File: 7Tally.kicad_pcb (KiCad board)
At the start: 4 copper layers, 22 parts, among them J1 53047-0210, P1 53047-0310, SW1 TL3300CF160Q, U1 ESP32-C3_SUPERMINI_TH, U2 BQ21040DBVR, U3 TC1263-3.3VOA

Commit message: chore(PCB): added 3D models and start PCB
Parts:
- removed D3: US1M, Diode_SMD:D_SMA
- removed J1: 53047-0210, 53047-0210:MOLEX_53047-0210
- added D4: ESD7351XV2T1G, ESD7351XV2T1G:SOD-523-2_ONSEMI, F.Cu at (24.7, 45.7)
- added J2: B2B-PH-K-S_LF__SN_, B2B-PH-K-S_LF__SN_:JST_B2B-PH-K-S_LF__SN_, B.Cu at (88.9, 73.7)
- moved U1 108.4 mm to (63.2, 63.5), turned to 90 degrees
- moved U2 72.9 mm to (80.0, 37.1)
- moved SW1 71.5 mm to (82.7, 63.3), turned to 180 degrees
- moved D1 56.0 mm to (72.7, 50.8), turned to 180 degrees
- moved P1 55.6 mm to (59.7, 52.6), turned to 180 degrees
- moved U3 29.5 mm to (61.0, 38.1)
- moved D2 13.6 mm to (26.3, 48.3)
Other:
- board outline added: 42 x 25.4 mm

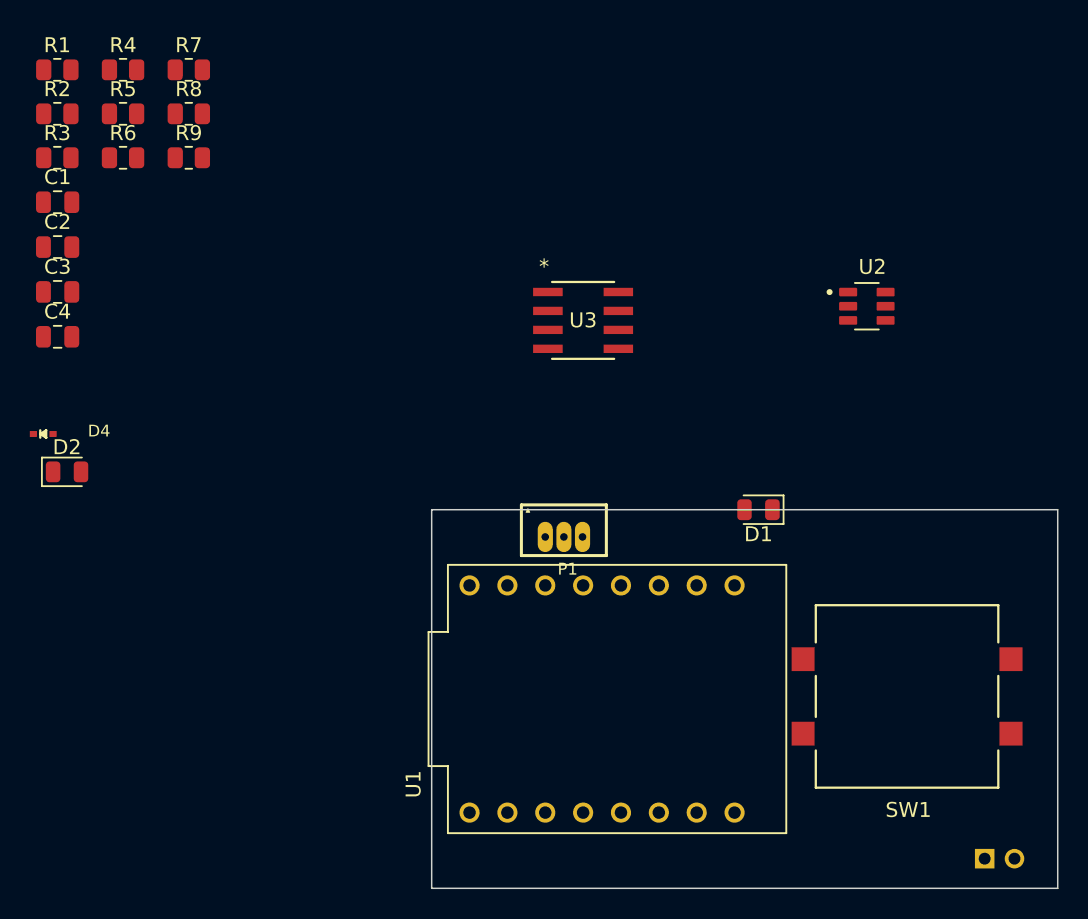
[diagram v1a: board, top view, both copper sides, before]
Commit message: feat(PCB): start of routing
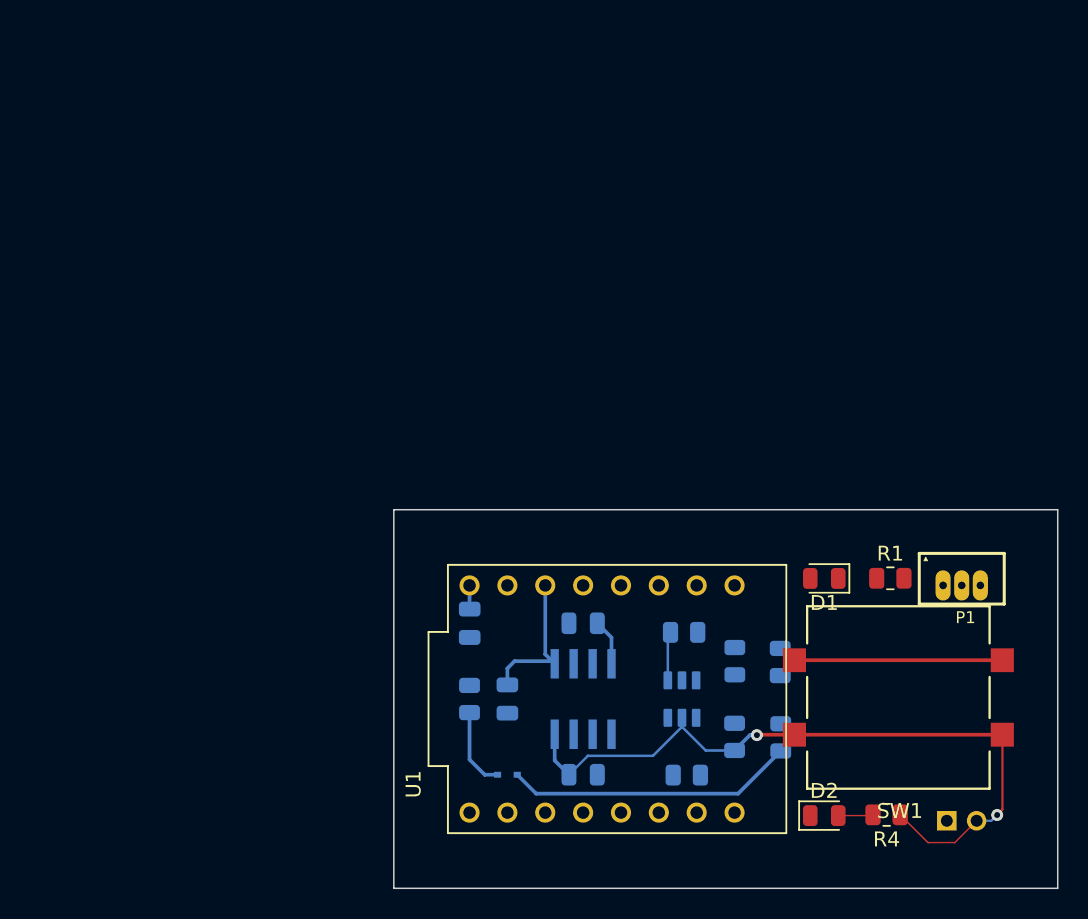
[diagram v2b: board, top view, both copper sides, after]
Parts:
- C1, C2, C3, C4, D4, R2, R3, R5, R6, R7, R8, R9, U2, U3: moved to B.Cu
- moved R4 71.6 mm to (81.3, 71.3), turned to 180 degrees
- moved R1 65.5 mm to (81.6, 55.4)
- moved R5 60.8 mm to (74.2, 66.1), turned to 90 degrees
- moved R3 59.1 mm to (67.9, 68.6), turned to 180 degrees
- moved R7 57.8 mm to (71.1, 66.0), turned to 90 degrees
- moved D2 55.8 mm to (77.1, 71.3)
- moved R6 55.6 mm to (74.2, 61.0), turned to 90 degrees
- moved R2 54.6 mm to (67.7, 59.0)
- moved C1 52.1 mm to (61.0, 68.6)
- moved R8 51.9 mm to (71.1, 61.0), turned to 90 degrees
- moved R9 40.9 mm to (53.3, 63.5), turned to 90 degrees
- moved C3 40.7 mm to (55.9, 63.5), turned to -90 degrees
- moved C4 40.2 mm to (61.0, 58.4), turned to 180 degrees
- moved D4 38.6 mm to (55.9, 68.6)
- moved C2 37.4 mm to (53.4, 58.4), turned to -90 degrees
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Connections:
- U3 pad 2: unconnected-(U3-GND-Pad2) -> GND
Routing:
- net VBAT: track 0.00 -> 48.8 mm, vias 0 -> 2
- net Net-(D4-Pad2): track 0.00 -> 33.3 mm
- net +3.3V: track 0.00 -> 10.1 mm
- net enablePort: track 0.00 -> 5.45 mm
- net Net-(U2-ISET): track 0.00 -> 3.29 mm
- net BP: track 0.00 -> 3.11 mm
- net Net-(D2-A): track 0.00 -> 2.35 mm
- net +5V: track 0.00 -> 1.59 mm
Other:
- board size 42 x 25.4 mm -> 44.5 x 25.4 mm

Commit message: feat(PCB): finished routing
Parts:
- moved R3 0.30 mm to (67.6, 68.5)
- moved R6 0.08 mm to (74.2, 61.1)
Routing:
- net +3.3V: track 10.1 -> 38.7 mm
- net NEOPIXEL_PIN: track 0.00 -> 19.8 mm
- net +5V: track 1.59 -> 20.2 mm, vias 0 -> 1
- net Net-(D2-K): track 0.00 -> 16.1 mm, vias 0 -> 1
- net socPin: track 0.00 -> 14.9 mm
- net enablePort: track 5.45 -> 17.7 mm, vias 0 -> 2
- net GP_LED: track 0.00 -> 11.6 mm
- net buttonPin: track 0.00 -> 10.6 mm
- net Net-(D4-Pad2): track 33.3 -> 42.4 mm, vias 0 -> 3
- net Net-(U2-TS): track 0.00 -> 3.75 mm
- net Net-(D1-K): track 0.00 -> 2.59 mm
- net VBAT: track 48.8 -> 51.4 mm

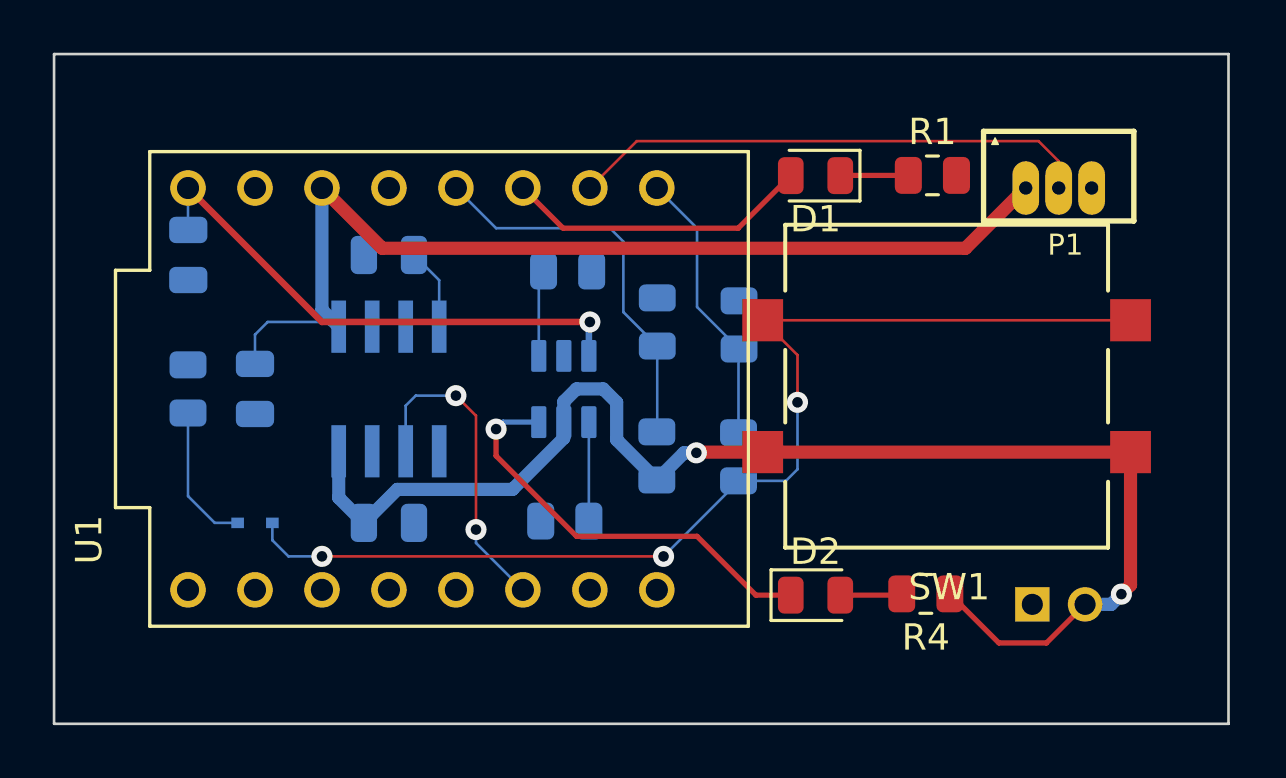
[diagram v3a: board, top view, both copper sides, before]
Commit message: feat(PCB): finished V1
First version fully connected - DRC missing
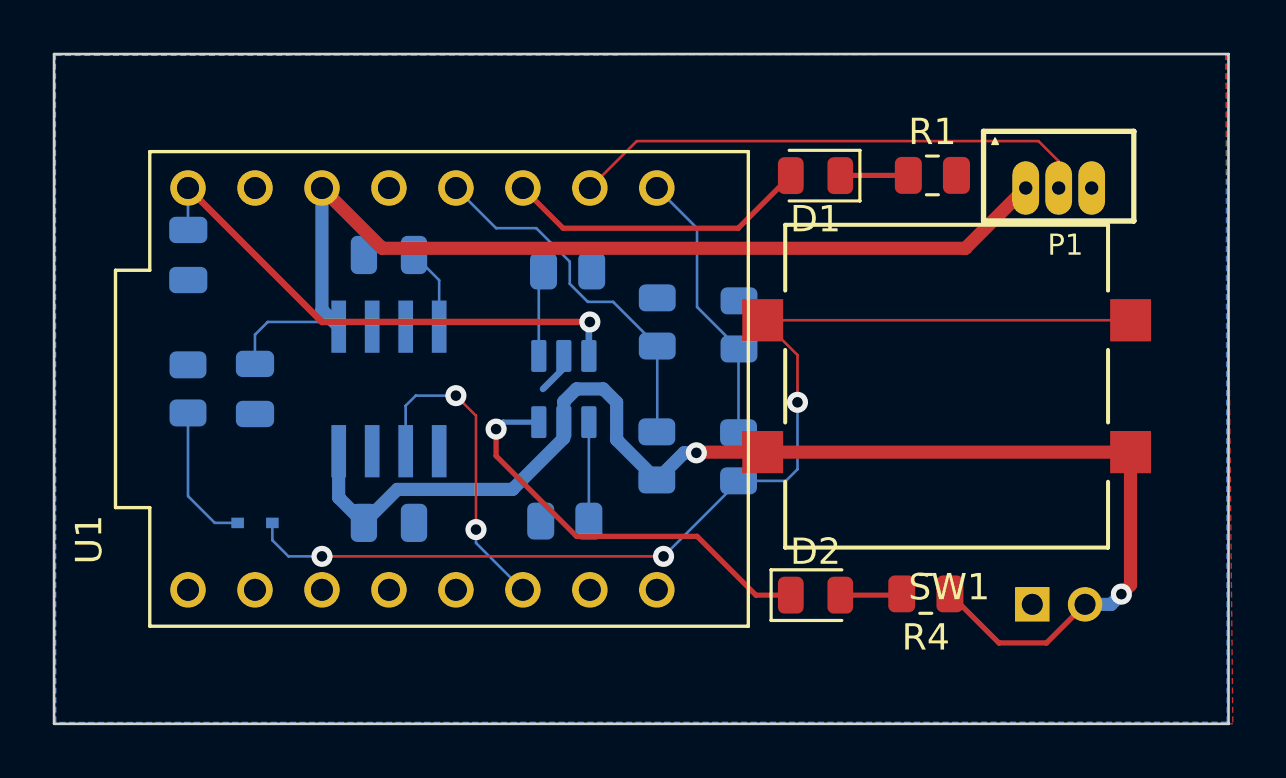
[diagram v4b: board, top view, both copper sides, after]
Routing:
- net GND: track 0.00 -> 1.66 mm
- net socPin: track 14.9 -> 13.9 mm
- added copper zone on B.Cu, net GND
- added copper zone on F.Cu, net GND
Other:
- copper layers 4 -> 2
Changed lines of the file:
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@@
 	(layers
 		(0 "F.Cu" signal)
-		(4 "In1.Cu" signal)
-		(6 "In2.Cu" signal)
 		(2 "B.Cu" signal)
 		(9 "F.Adhes" user "F.Adhesive")
@@
 			)
 			(layer "dielectric 1"
-				(type "prepreg")
-				(thickness 0.1)
-				(material "FR4")
-				(epsilon_r 4.5)
-				(loss_tangent 0.02)
-			)
-			(layer "In1.Cu"
-				(type "copper")
-				(thickness 0.035)
-			)
-			(layer "dielectric 2"
 				(type "core")
-				(thickness 1.24)
-				(material "FR4")
-				(epsilon_r 4.5)
-				(loss_tangent 0.02)
-			)
-			(layer "In2.Cu"
-				(type "copper")
-				(thickness 0.035)
-			)
-			(layer "dielectric 3"
-				(type "prepreg")
-				(thickness 0.1)
+				(thickness 1.51)
 				(material "FR4")
 				(epsilon_r 4.5)
@@
 	)
 	(segment
+		(start 67.592687 62.248686)
+		(end 67.592687 62.709313)
+		(width 0.17)
+		(layer "B.Cu")
+		(net 1)
+	)
+	(segment
+		(start 68.648129 59.113871)
+		(end 68.648129 59.028893)
+		(width 0.17)
+		(layer "B.Cu")
+		(net 1)
+	)
+	(segment
+		(start 67.592687 62.709313)
+		(end 66.802 63.5)
+		(width 0.25)
+		(layer "B.Cu")
+		(net 1)
+	)
+	(segment
 		(start 75.135066 65.896241)
 		(end 89.085066 65.896241)
@@
 	)
 	(segment
-		(start 69.85 57.912)
-		(end 69.342 57.404)
+		(start 71.136679 61.8725)
+		(end 71.136679 65.110821)
 		(width 0.1)
 		(layer "B.Cu")
@@
 	)
 	(segment
-		(start 71.136679 61.8725)
-		(end 71.136679 65.110821)
+		(start 66.548 57.404)
+		(end 65.024 57.404)
 		(width 0.1)
 		(layer "B.Cu")
@@
 	)
 	(segment
-		(start 69.342 57.404)
-		(end 65.024 57.404)
+		(start 67.818 59.513574)
+		(end 67.818 58.674)
+		(width 0.1)
+		(layer "B.Cu")
+		(net 16)
+	)
+	(segment
+		(start 69.462179 60.198)
+		(end 68.502426 60.198)
 		(width 0.1)
 		(layer "B.Cu")
@@
 	)
 	(segment
-		(start 69.85 60.585821)
-		(end 69.85 57.912)
+		(start 67.818 58.674)
+		(end 66.548 57.404)
+		(width 0.1)
+		(layer "B.Cu")
+		(net 16)
+	)
+	(segment
+		(start 68.502426 60.198)
+		(end 67.818 59.513574)
 		(width 0.1)
 		(layer "B.Cu")
@@
 	(segment
 		(start 71.136679 61.8725)
-		(end 69.85 60.585821)
+		(end 69.462179 60.198)
 		(width 0.1)
 		(layer "B.Cu")
 		(net 16)
 	)
+	(zone
+		(net 1)
+		(net_name "GND")
+		(layer "F.Cu")
+		(hatch edge 0.5)
+		(connect_pads
+			(clearance 0.5)
+		)
+		(min_thickness 0.25)
+		(filled_areas_thickness no)
+		(fill yes
+			(thermal_gap 0.5)
+			(thermal_bridge_width 0.5)
+		)
+		(polygon
+			(pts
+				(xy 92.71 50.8) (xy 92.964 76.2) (xy 48.26 76.2) (xy 48.26 50.8)
+			)
+		)
+	)
+	(zone
+		(net 1)
+		(net_name "GND")
+		(layer "B.Cu")
+		(hatch edge 0.5)
+		(priority 1)
+		(connect_pads
+			(clearance 0.5)
+		)
+		(min_thickness 0.25)
+		(filled_areas_thickness no)
+		(fill yes
+			(thermal_gap 0.5)
+			(thermal_bridge_width 0.5)
+		)
+		(polygon
+			(pts
+				(xy 92.71 50.8) (xy 92.746105 76.137977) (xy 48.326137 76.148214) (xy 48.312238 50.851353)
+			)
+		)
+	)
 	(embedded_fonts no)

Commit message: chore(PCB): Passed DRC
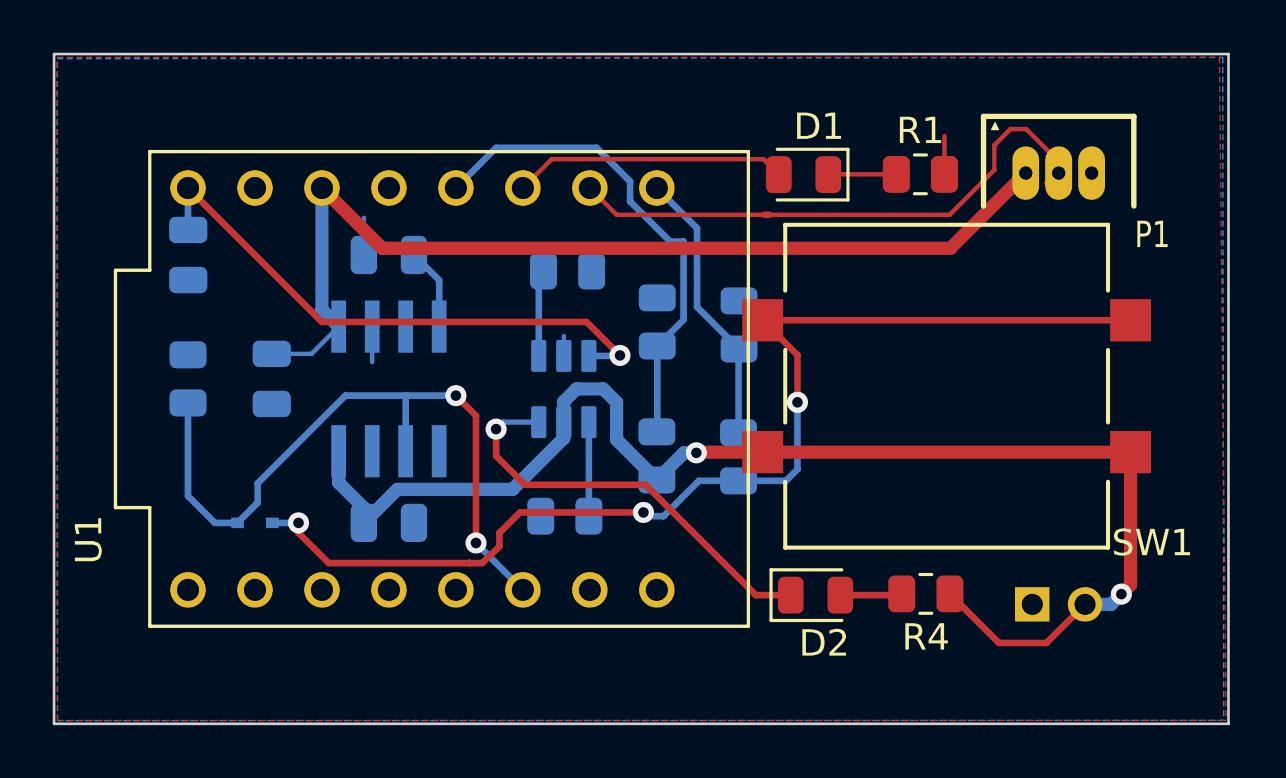
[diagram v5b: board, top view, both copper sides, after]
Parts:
- moved C3 0.74 mm to (56.5, 63.1)
- moved P1 0.57 mm to (86.4, 55.3)
- moved D1 0.46 mm to (76.7, 55.4)
- moved R1 0.46 mm to (81.1, 55.4)
- moved R9 0.38 mm to (53.3, 63.1)
- moved R3 0.19 mm to (67.6, 68.3)
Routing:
- net enablePort: track 17.7 -> 26.7 mm
- net socPin: track 13.9 -> 18.8 mm
- net GND: track 1.66 -> 5.50 mm
- net NEOPIXEL_PIN: track 19.8 -> 22.0 mm
- net +5V: track 20.2 -> 21.8 mm
- net GP_LED: track 11.6 -> 10.4 mm
- net +3.3V: track 38.7 -> 37.9 mm

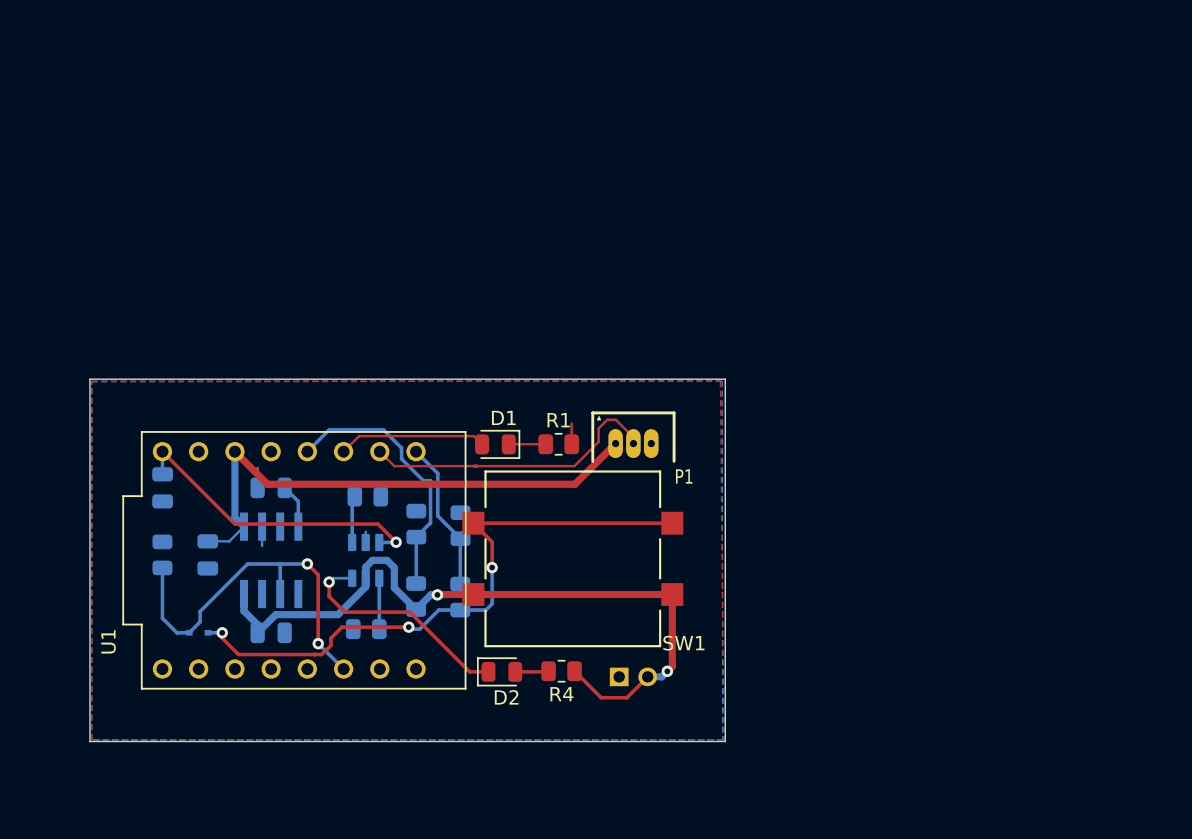
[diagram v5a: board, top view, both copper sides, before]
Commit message: feat(PCB): Start leds
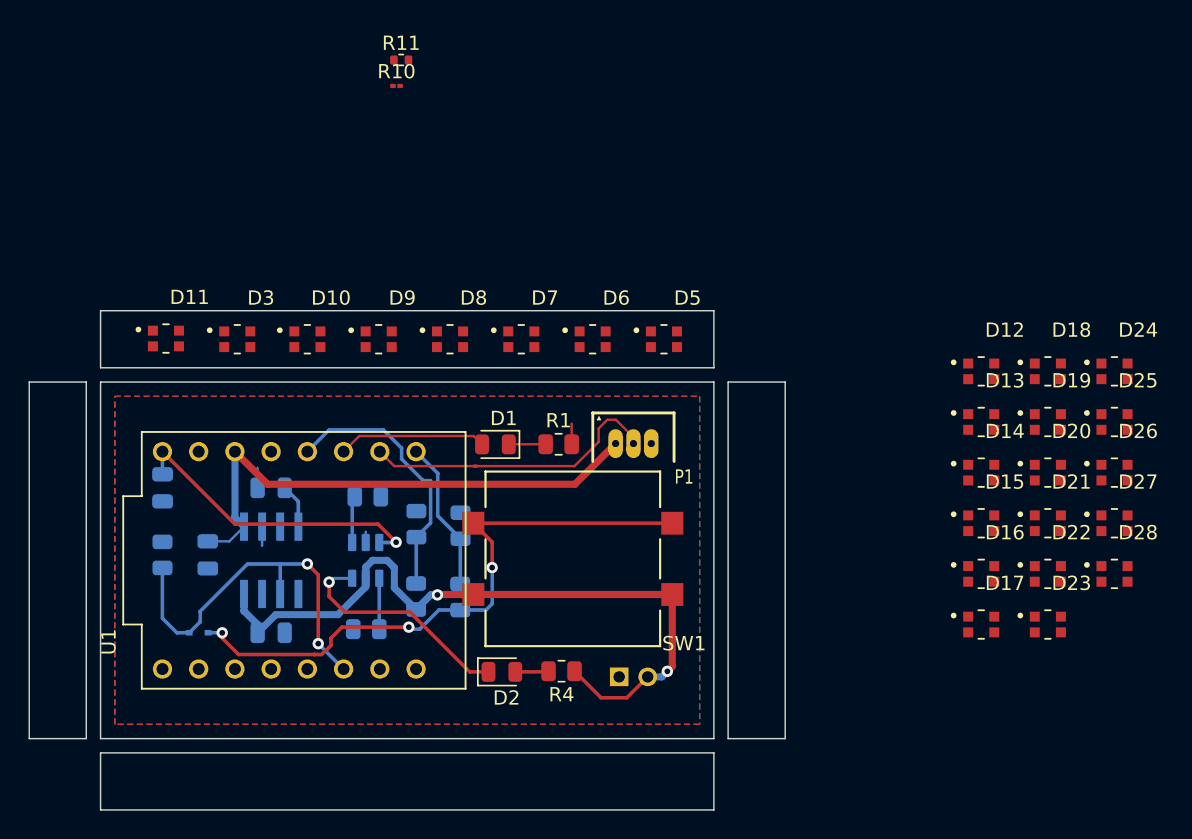
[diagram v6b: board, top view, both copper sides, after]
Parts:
- added D10: WS2812B2020, WS2812B2020:LED_WS2812B2020, F.Cu at (63.5, 48.0)
- added D11: WS2812B2020, WS2812B2020:LED_WS2812B2020, F.Cu at (53.6, 48.0)
- added D12: WS2812B2020, WS2812B2020:LED_WS2812B2020, F.Cu at (110.7, 50.2)
- added D13: WS2812B2020, WS2812B2020:LED_WS2812B2020, F.Cu at (110.7, 53.8)
- added D14: WS2812B2020, WS2812B2020:LED_WS2812B2020, F.Cu at (110.7, 57.4)
- added D15: WS2812B2020, WS2812B2020:LED_WS2812B2020, F.Cu at (110.7, 60.9)
- added D16: WS2812B2020, WS2812B2020:LED_WS2812B2020, F.Cu at (110.7, 64.5)
- added D17: WS2812B2020, WS2812B2020:LED_WS2812B2020, F.Cu at (110.7, 68.0)
- added D18: WS2812B2020, WS2812B2020:LED_WS2812B2020, F.Cu at (115.4, 50.2)
- added D19: WS2812B2020, WS2812B2020:LED_WS2812B2020, F.Cu at (115.4, 53.8)
- added D20: WS2812B2020, WS2812B2020:LED_WS2812B2020, F.Cu at (115.4, 57.4)
- added D21: WS2812B2020, WS2812B2020:LED_WS2812B2020, F.Cu at (115.4, 60.9)
- added D22: WS2812B2020, WS2812B2020:LED_WS2812B2020, F.Cu at (115.4, 64.5)
- added D23: WS2812B2020, WS2812B2020:LED_WS2812B2020, F.Cu at (115.4, 68.0)
- added D24: WS2812B2020, WS2812B2020:LED_WS2812B2020, F.Cu at (120.1, 50.2)
- added D25: WS2812B2020, WS2812B2020:LED_WS2812B2020, F.Cu at (120.1, 53.8)
- added D26: WS2812B2020, WS2812B2020:LED_WS2812B2020, F.Cu at (120.1, 57.4)
- added D27: WS2812B2020, WS2812B2020:LED_WS2812B2020, F.Cu at (120.1, 60.9)
- added D28: WS2812B2020, WS2812B2020:LED_WS2812B2020, F.Cu at (120.1, 64.5)
- added D3: WS2812B2020, WS2812B2020:LED_WS2812B2020, F.Cu at (58.6, 48.0)
- added D5: WS2812B2020, WS2812B2020:LED_WS2812B2020, F.Cu at (88.5, 48.0)
- added D6: WS2812B2020, WS2812B2020:LED_WS2812B2020, F.Cu at (83.5, 48.0)
- added D7: WS2812B2020, WS2812B2020:LED_WS2812B2020, F.Cu at (78.5, 48.0)
- added D8: WS2812B2020, WS2812B2020:LED_WS2812B2020, F.Cu at (73.5, 48.0)
- added D9: WS2812B2020, WS2812B2020:LED_WS2812B2020, F.Cu at (68.5, 48.0)
- added R10: 0, Resistor_SMD:R_01005_0402Metric, F.Cu at (69.7, 30.2)
- added R11: 0, Resistor_SMD:R_0402_1005Metric, F.Cu at (70.1, 28.4)
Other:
- board size 44.5 x 25.4 mm -> 53 x 35 mm
